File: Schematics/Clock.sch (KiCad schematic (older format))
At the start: 27 parts, among them SW1 SW_Push, U66 LM555, U67 74LS393, U68 74LS04, U69 74LS393, U70 74LS151, U71 74LS393, U72 74LS393, U73 74LS393, U74 74LS393

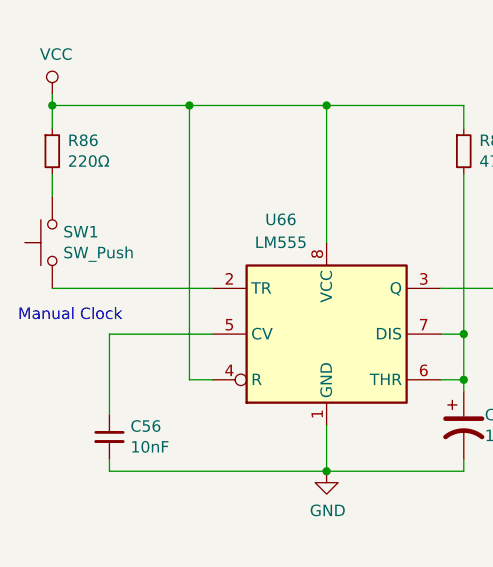
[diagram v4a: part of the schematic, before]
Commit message: Assign a bunch of part footprints.
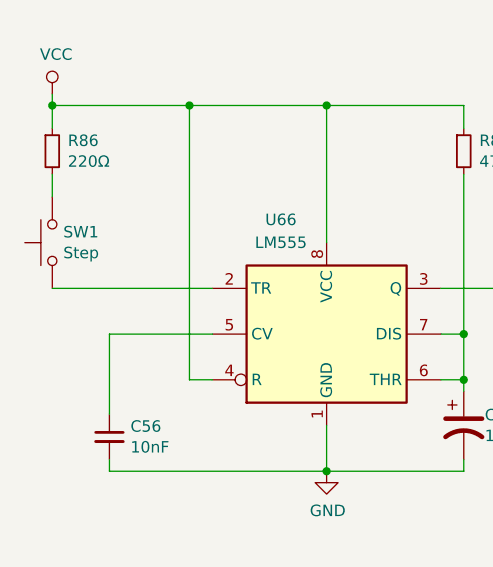
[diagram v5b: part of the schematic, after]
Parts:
- D72: footprint (none) -> LED_THT:LED_D5.0mm
- R86, R87, R88: footprint (none) -> Resistor_THT:R_Axial_DIN0207_L6.3mm_D2.5mm_P7.62mm_Horizontal
- SW1: value SW_Push -> Step; footprint (none) -> Button_Switch_THT:SW_PUSH_6mm_H5mm
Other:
- note removed: "Manual Clock"
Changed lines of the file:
@@
 F 0 "R88" H 5118 6046 50  0000 L CNN
 F 1 "220Ω" H 5118 5955 50  0000 L CNN
-F 2 "" V 5090 5990 50  0001 C CNN
+F 2 "Resistor_THT:R_Axial_DIN0207_L6.3mm_D2.5mm_P7.62mm_Horizontal" V 5090 5990 50  0001 C CNN
 F 3 "~" H 5050 6000 50  0001 C CNN
 	1    5050 6000
@@
 F 0 "D72" V 5089 5433 50  0000 R CNN
 F 1 "LED" V 4998 5433 50  0000 R CNN
-F 2 "" H 5050 5550 50  0001 C CNN
+F 2 "LED_THT:LED_D5.0mm" H 5050 5550 50  0001 C CNN
 F 3 "~" H 5050 5550 50  0001 C CNN
 	1    5050 5550
@@
 F 0 "R87" H 2668 3396 50  0000 L CNN
 F 1 "47kΩ" H 2668 3305 50  0000 L CNN
-F 2 "" H 2600 3350 50  0001 C CNN
+F 2 "Resistor_THT:R_Axial_DIN0207_L6.3mm_D2.5mm_P7.62mm_Horizontal" H 2600 3350 50  0001 C CNN
 F 3 "~" H 2600 3350 50  0001 C CNN
 	1    2600 3350
@@
 F 0 "R86" H 868 3396 50  0000 L CNN
 F 1 "220Ω" H 868 3305 50  0000 L CNN
-F 2 "" H 800 3350 50  0001 C CNN
+F 2 "Resistor_THT:R_Axial_DIN0207_L6.3mm_D2.5mm_P7.62mm_Horizontal" H 800 3350 50  0001 C CNN
 F 3 "~" H 800 3350 50  0001 C CNN
 	1    800  3350
@@
 P 800 3750
 F 0 "SW1" V 846 3702 50  0000 R CNN
-F 1 "SW_Push" V 755 3702 50  0000 R CNN
-F 2 "" H 800 3950 50  0001 C CNN
+F 1 "Step" V 755 3702 50  0000 R CNN
+F 2 "Button_Switch_THT:SW_PUSH_6mm_H5mm" H 800 3950 50  0001 C CNN
 F 3 "~" H 800 3950 50  0001 C CNN
 	1    800  3750
 	0    -1   -1   0
 $EndComp
-Text Notes 650  4100 0    50   ~ 0
-Manual Clock
 Wire Wire Line
 	3650 5200 3150 5200

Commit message: Assign a bunch more footprints. All are assigned now.
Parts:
- U66: footprint (none) -> Package_DIP:DIP-8_W7.62mm
- U67, U68, U69, U71, U72, U73, U74: footprint (none) -> Package_DIP:DIP-14_W7.62mm
- U70: footprint (none) -> Package_DIP:DIP-16_W7.62mm
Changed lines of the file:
@@
 F 0 "U67" H 2550 1917 50  0000 C CNN
 F 1 "74LS393" H 2550 1826 50  0000 C CNN
-F 2 "" H 2550 1550 50  0001 C CNN
+F 2 "Package_DIP:DIP-14_W7.62mm" H 2550 1550 50  0001 C CNN
 F 3 "74xx\\74LS393.pdf" H 2550 1550 50  0001 C CNN
 	1    2550 1550
@@
 F 0 "U71" H 5300 1917 50  0000 C CNN
 F 1 "74LS393" H 5300 1826 50  0000 C CNN
-F 2 "" H 5300 1550 50  0001 C CNN
+F 2 "Package_DIP:DIP-14_W7.62mm" H 5300 1550 50  0001 C CNN
 F 3 "74xx\\74LS393.pdf" H 5300 1550 50  0001 C CNN
 	1    5300 1550
@@
 F 0 "U72" H 6600 1917 50  0000 C CNN
 F 1 "74LS393" H 6600 1826 50  0000 C CNN
-F 2 "" H 6600 1550 50  0001 C CNN
+F 2 "Package_DIP:DIP-14_W7.62mm" H 6600 1550 50  0001 C CNN
 F 3 "74xx\\74LS393.pdf" H 6600 1550 50  0001 C CNN
 	1    6600 1550
@@
 F 0 "U73" H 7950 1917 50  0000 C CNN
 F 1 "74LS393" H 7950 1826 50  0000 C CNN
-F 2 "" H 7950 1550 50  0001 C CNN
+F 2 "Package_DIP:DIP-14_W7.62mm" H 7950 1550 50  0001 C CNN
 F 3 "74xx\\74LS393.pdf" H 7950 1550 50  0001 C CNN
 	1    7950 1550
@@
 F 0 "U74" H 9350 1917 50  0000 C CNN
 F 1 "74LS393" H 9350 1826 50  0000 C CNN
-F 2 "" H 9350 1550 50  0001 C CNN
+F 2 "Package_DIP:DIP-14_W7.62mm" H 9350 1550 50  0001 C CNN
 F 3 "74xx\\74LS393.pdf" H 9350 1550 50  0001 C CNN
 	1    9350 1550
@@
 F 0 "U69" H 3900 1917 50  0000 C CNN
 F 1 "74LS393" H 3900 1826 50  0000 C CNN
-F 2 "" H 3900 1550 50  0001 C CNN
+F 2 "Package_DIP:DIP-14_W7.62mm" H 3900 1550 50  0001 C CNN
 F 3 "74xx\\74LS393.pdf" H 3900 1550 50  0001 C CNN
 	1    3900 1550
@@
 F 0 "U70" H 3900 6400 50  0000 C CNN
 F 1 "74LS151" H 3900 6300 50  0000 C CNN
-F 2 "" H 4150 5500 50  0001 C CNN
+F 2 "Package_DIP:DIP-16_W7.62mm" H 4150 5500 50  0001 C CNN
 F 3 "http://www.ti.com/lit/gpn/sn74LS151" H 4150 5500 50  0001 C CNN
 	1    4150 5500
@@
 F 0 "U68" H 2800 6767 50  0000 C CNN
 F 1 "74LS04" H 2800 6676 50  0000 C CNN
-F 2 "" H 2800 6450 50  0001 C CNN
+F 2 "Package_DIP:DIP-14_W7.62mm" H 2800 6450 50  0001 C CNN
 F 3 "http://www.ti.com/lit/gpn/sn74LS04" H 2800 6450 50  0001 C CNN
 	1    2800 6450
@@
 F 0 "U66" H 1800 4650 50  0000 C CNN
 F 1 "LM555" H 1800 4550 50  0000 C CNN
-F 2 "" H 2000 4150 50  0001 C CNN
+F 2 "Package_DIP:DIP-8_W7.62mm" H 2000 4150 50  0001 C CNN
 F 3 "http://www.ti.com/lit/ds/symlink/lm555.pdf" H 2000 4150 50  0001 C CNN
 	1    2000 4150

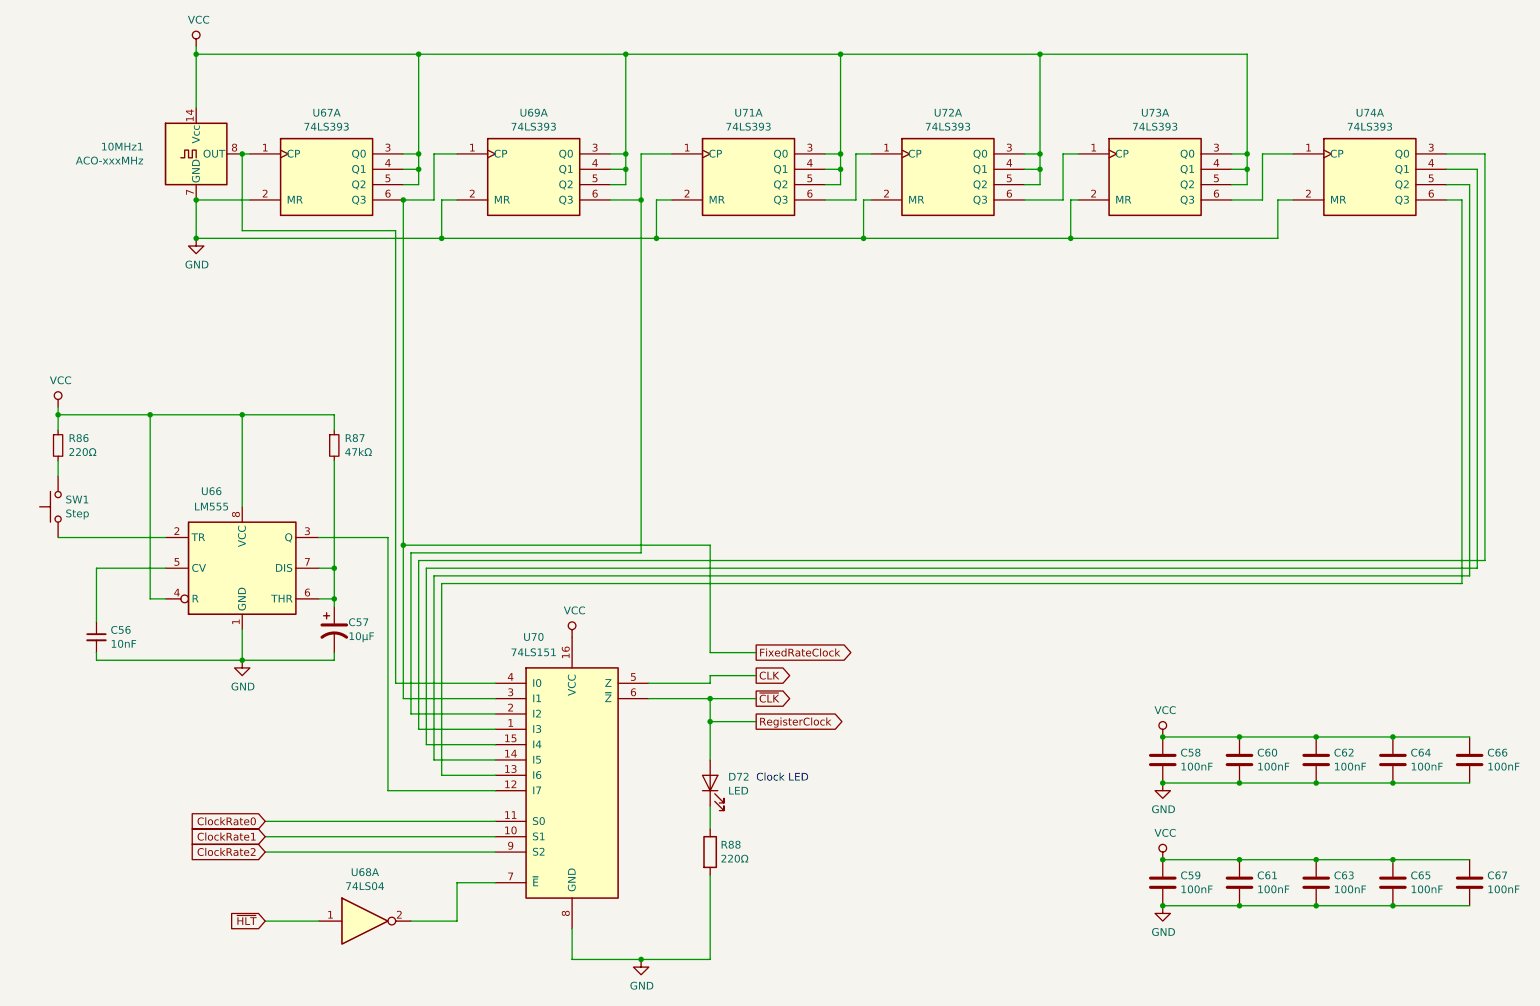
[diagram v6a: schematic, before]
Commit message: Add unused IC units to Output Display to ensure no ICs are shared with other modules.
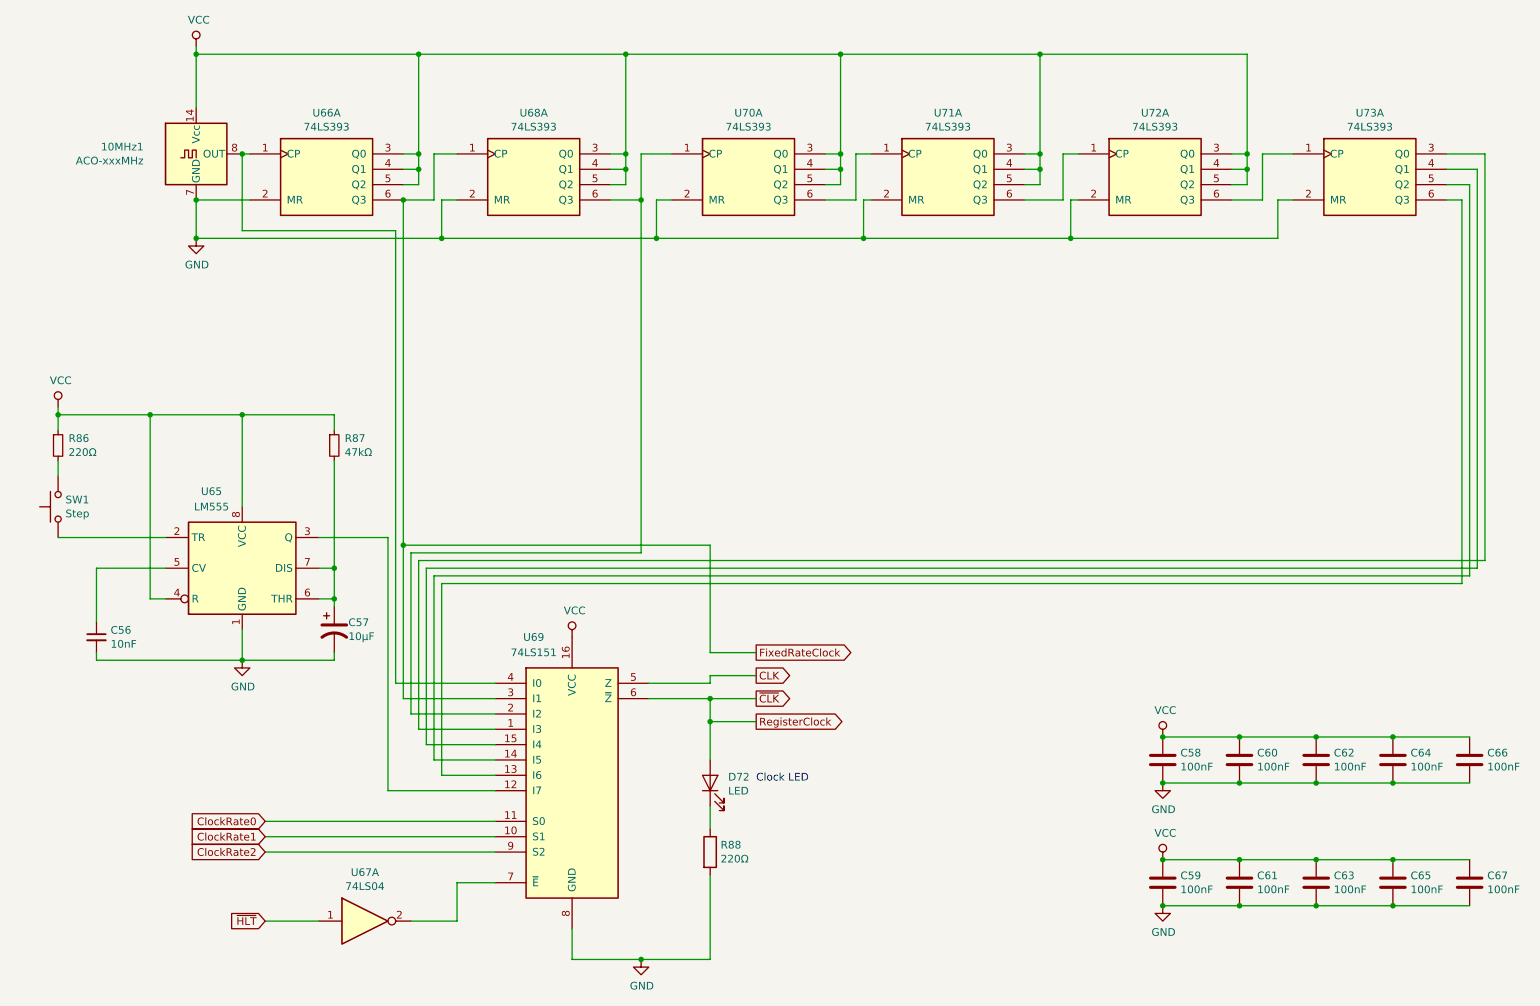
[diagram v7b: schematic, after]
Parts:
- renumbered U66 to U65, U67 to U66, U68 to U67, U69 to U68, U70 to U69, U71 to U70, U72 to U71, U73 to U72, U74 to U73
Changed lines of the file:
@@
 $EndComp
 $Comp
-L 74xx:74LS393 U67
+L 74xx:74LS393 U66
 U 1 1 5D3898BC
 P 2550 1550
-F 0 "U67" H 2550 1917 50  0000 C CNN
+F 0 "U66" H 2550 1917 50  0000 C CNN
 F 1 "74LS393" H 2550 1826 50  0000 C CNN
 F 2 "Package_DIP:DIP-14_W7.62mm" H 2550 1550 50  0001 C CNN
@@
 $EndComp
 $Comp
-L 74xx:74LS393 U71
+L 74xx:74LS393 U70
 U 1 1 5D38C231
 P 5300 1550
-F 0 "U71" H 5300 1917 50  0000 C CNN
+F 0 "U70" H 5300 1917 50  0000 C CNN
 F 1 "74LS393" H 5300 1826 50  0000 C CNN
 F 2 "Package_DIP:DIP-14_W7.62mm" H 5300 1550 50  0001 C CNN
@@
 $EndComp
 $Comp
-L 74xx:74LS393 U72
+L 74xx:74LS393 U71
 U 1 1 5D38D960
 P 6600 1550
-F 0 "U72" H 6600 1917 50  0000 C CNN
+F 0 "U71" H 6600 1917 50  0000 C CNN
 F 1 "74LS393" H 6600 1826 50  0000 C CNN
 F 2 "Package_DIP:DIP-14_W7.62mm" H 6600 1550 50  0001 C CNN
@@
 $EndComp
 $Comp
-L 74xx:74LS393 U73
+L 74xx:74LS393 U72
 U 1 1 5D38E544
 P 7950 1550
-F 0 "U73" H 7950 1917 50  0000 C CNN
+F 0 "U72" H 7950 1917 50  0000 C CNN
 F 1 "74LS393" H 7950 1826 50  0000 C CNN
 F 2 "Package_DIP:DIP-14_W7.62mm" H 7950 1550 50  0001 C CNN
@@
 	7350 1450 7450 1450
 $Comp
-L 74xx:74LS393 U74
+L 74xx:74LS393 U73
 U 1 1 5D3C15D2
 P 9350 1550
-F 0 "U74" H 9350 1917 50  0000 C CNN
+F 0 "U73" H 9350 1917 50  0000 C CNN
 F 1 "74LS393" H 9350 1826 50  0000 C CNN
 F 2 "Package_DIP:DIP-14_W7.62mm" H 9350 1550 50  0001 C CNN
@@
 Connection ~ 7200 800
 $Comp
-L 74xx:74LS393 U69
+L 74xx:74LS393 U68
 U 1 1 5D38B39F
 P 3900 1550
-F 0 "U69" H 3900 1917 50  0000 C CNN
+F 0 "U68" H 3900 1917 50  0000 C CNN
 F 1 "74LS393" H 3900 1826 50  0000 C CNN
 F 2 "Package_DIP:DIP-14_W7.62mm" H 3900 1550 50  0001 C CNN
@@
 	1700 1750 2050 1750
 $Comp
-L 74xx:74LS151 U70
+L 74xx:74LS151 U69
 U 1 1 5D3FEA17
 P 4150 5500
-F 0 "U70" H 3900 6400 50  0000 C CNN
+F 0 "U69" H 3900 6400 50  0000 C CNN
 F 1 "74LS151" H 3900 6300 50  0000 C CNN
 F 2 "Package_DIP:DIP-16_W7.62mm" H 4150 5500 50  0001 C CNN
@@
 	5050 4850 5350 4850
 $Comp
-L power:VCC #PWR0249
+L power:VCC #PWR0153
 U 1 1 5D90C7E6
 P 4150 4600
-F 0 "#PWR0249" H 4150 4450 50  0001 C CNN
+F 0 "#PWR0153" H 4150 4450 50  0001 C CNN
 F 1 "VCC" H 4167 4773 50  0000 C CNN
 F 2 "" H 4150 4600 50  0001 C CNN
@@
 $EndComp
 $Comp
-L power:GND #PWR0250
+L power:GND #PWR0152
 U 1 1 5D919C2F
 P 2000 4750
-F 0 "#PWR0250" H 2000 4500 50  0001 C CNN
+F 0 "#PWR0152" H 2000 4500 50  0001 C CNN
 F 1 "GND" H 2005 4577 50  0000 C CNN
 F 2 "" H 2000 4750 50  0001 C CNN
@@
 $EndComp
 $Comp
-L power:GND #PWR0251
+L power:GND #PWR0154
 U 1 1 5D91A0CA
 P 4600 6700
-F 0 "#PWR0251" H 4600 6450 50  0001 C CNN
+F 0 "#PWR0154" H 4600 6450 50  0001 C CNN
 F 1 "GND" H 4605 6527 50  0000 C CNN
 F 2 "" H 4600 6700 50  0001 C CNN
@@
 $EndComp
 $Comp
-L power:GND #PWR0252
+L power:GND #PWR0156
 U 1 1 5D936CDD
 P 8000 5550
-F 0 "#PWR0252" H 8000 5300 50  0001 C CNN
+F 0 "#PWR0156" H 8000 5300 50  0001 C CNN
 F 1 "GND" H 8005 5377 50  0000 C CNN
 F 2 "" H 8000 5550 50  0001 C CNN
@@
 $EndComp
 $Comp
-L power:VCC #PWR0253
+L power:VCC #PWR0155
 U 1 1 5D937A39
 P 8000 5250
-F 0 "#PWR0253" H 8000 5100 50  0001 C CNN
+F 0 "#PWR0155" H 8000 5100 50  0001 C CNN
 F 1 "VCC" H 8017 5423 50  0000 C CNN
 F 2 "" H 8000 5250 50  0001 C CNN
@@
 $EndComp
 $Comp
-L power:GND #PWR0254
+L power:GND #PWR0158
 U 1 1 5D9721F9
 P 8000 6350
-F 0 "#PWR0254" H 8000 6100 50  0001 C CNN
+F 0 "#PWR0158" H 8000 6100 50  0001 C CNN
 F 1 "GND" H 8005 6177 50  0000 C CNN
 F 2 "" H 8000 6350 50  0001 C CNN
@@
 $EndComp
 $Comp
-L power:VCC #PWR0255
+L power:VCC #PWR0157
 U 1 1 5D9721FF
 P 8000 6050
-F 0 "#PWR0255" H 8000 5900 50  0001 C CNN
+F 0 "#PWR0157" H 8000 5900 50  0001 C CNN
 F 1 "VCC" H 8017 6223 50  0000 C CNN
 F 2 "" H 8000 6050 50  0001 C CNN
@@
 	3300 1750 3300 2000
 $Comp
-L power:GND #PWR0256
+L power:GND #PWR0151
 U 1 1 5D888695
 P 1700 2000
-F 0 "#PWR0256" H 1700 1750 50  0001 C CNN
+F 0 "#PWR0151" H 1700 1750 50  0001 C CNN
 F 1 "GND" H 1705 1827 50  0000 C CNN
 F 2 "" H 1700 2000 50  0001 C CNN
@@
 	1700 2000 3300 2000
 $Comp
-L power:VCC #PWR0257
+L power:VCC #PWR0150
 U 1 1 5D3986DC
 P 1700 750
-F 0 "#PWR0257" H 1700 600 50  0001 C CNN
+F 0 "#PWR0150" H 1700 600 50  0001 C CNN
 F 1 "VCC" H 1717 923 50  0000 C CNN
 F 2 "" H 1700 750 50  0001 C CNN
@@
 	1700 750  1700 800
 $Comp
-L power:VCC #PWR0258
+L power:VCC #PWR0149
 U 1 1 5D8FB444
 P 800 3100
-F 0 "#PWR0258" H 800 2950 50  0001 C CNN
+F 0 "#PWR0149" H 800 2950 50  0001 C CNN
 F 1 "VCC" H 817 3273 50  0000 C CNN
 F 2 "" H 800 3100 50  0001 C CNN
@@
 	3100 6450 3400 6450
 $Comp
-L 74xx:74LS04 U68
+L 74xx:74LS04 U67
 U 1 1 5D7C9FC5
 P 2800 6450
-F 0 "U68" H 2800 6767 50  0000 C CNN
+F 0 "U67" H 2800 6767 50  0000 C CNN
 F 1 "74LS04" H 2800 6676 50  0000 C CNN
 F 2 "Package_DIP:DIP-14_W7.62mm" H 2800 6450 50  0001 C CNN
@@
 	4600 6700 5050 6700
 $Comp
-L Timer:LM555 U66
+L Timer:LM555 U65
 U 1 1 5D38F3A1
 P 2000 4150
-F 0 "U66" H 1800 4650 50  0000 C CNN
+F 0 "U65" H 1800 4650 50  0000 C CNN
 F 1 "LM555" H 1800 4550 50  0000 C CNN
 F 2 "Package_DIP:DIP-8_W7.62mm" H 2000 4150 50  0001 C CNN

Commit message: Add unused IC units to Data RAM to ensure no ICs are shared with other modules.
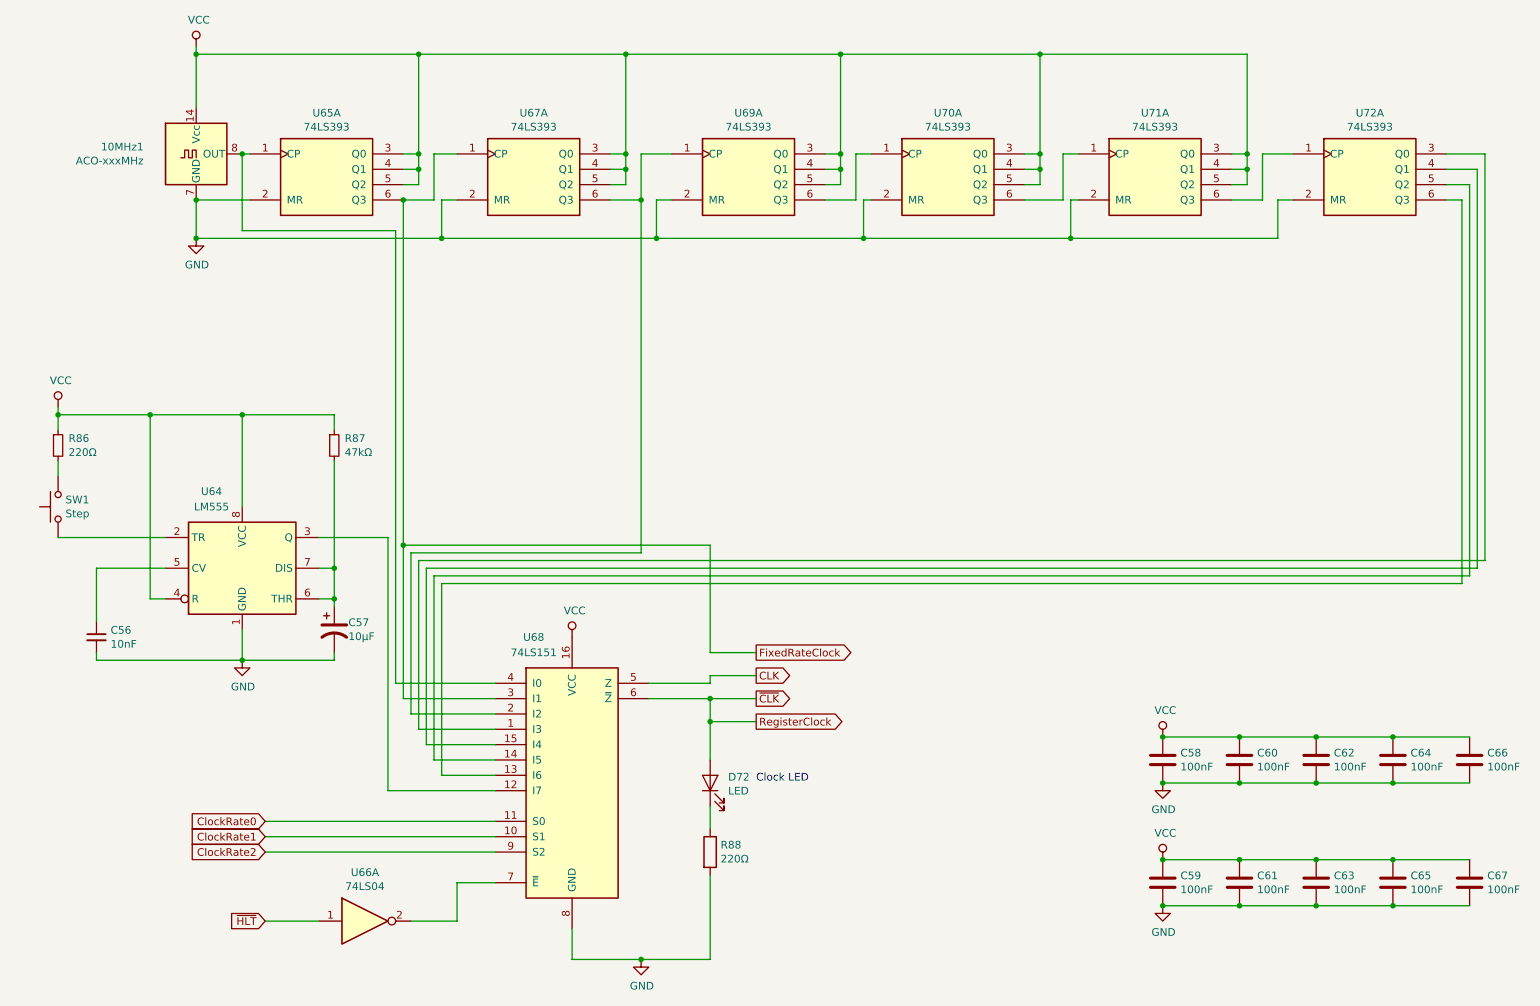
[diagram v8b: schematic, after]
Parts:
- renumbered U65 to U64, U66 to U65, U67 to U66, U68 to U67, U69 to U68, U70 to U69, U71 to U70, U72 to U71, U73 to U72
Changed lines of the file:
@@
 $EndComp
 $Comp
-L 74xx:74LS393 U66
+L 74xx:74LS393 U65
 U 1 1 5D3898BC
 P 2550 1550
-F 0 "U66" H 2550 1917 50  0000 C CNN
+F 0 "U65" H 2550 1917 50  0000 C CNN
 F 1 "74LS393" H 2550 1826 50  0000 C CNN
 F 2 "Package_DIP:DIP-14_W7.62mm" H 2550 1550 50  0001 C CNN
@@
 $EndComp
 $Comp
-L 74xx:74LS393 U70
+L 74xx:74LS393 U69
 U 1 1 5D38C231
 P 5300 1550
-F 0 "U70" H 5300 1917 50  0000 C CNN
+F 0 "U69" H 5300 1917 50  0000 C CNN
 F 1 "74LS393" H 5300 1826 50  0000 C CNN
 F 2 "Package_DIP:DIP-14_W7.62mm" H 5300 1550 50  0001 C CNN
@@
 $EndComp
 $Comp
-L 74xx:74LS393 U71
+L 74xx:74LS393 U70
 U 1 1 5D38D960
 P 6600 1550
-F 0 "U71" H 6600 1917 50  0000 C CNN
+F 0 "U70" H 6600 1917 50  0000 C CNN
 F 1 "74LS393" H 6600 1826 50  0000 C CNN
 F 2 "Package_DIP:DIP-14_W7.62mm" H 6600 1550 50  0001 C CNN
@@
 $EndComp
 $Comp
-L 74xx:74LS393 U72
+L 74xx:74LS393 U71
 U 1 1 5D38E544
 P 7950 1550
-F 0 "U72" H 7950 1917 50  0000 C CNN
+F 0 "U71" H 7950 1917 50  0000 C CNN
 F 1 "74LS393" H 7950 1826 50  0000 C CNN
 F 2 "Package_DIP:DIP-14_W7.62mm" H 7950 1550 50  0001 C CNN
@@
 	7350 1450 7450 1450
 $Comp
-L 74xx:74LS393 U73
+L 74xx:74LS393 U72
 U 1 1 5D3C15D2
 P 9350 1550
-F 0 "U73" H 9350 1917 50  0000 C CNN
+F 0 "U72" H 9350 1917 50  0000 C CNN
 F 1 "74LS393" H 9350 1826 50  0000 C CNN
 F 2 "Package_DIP:DIP-14_W7.62mm" H 9350 1550 50  0001 C CNN
@@
 Connection ~ 7200 800
 $Comp
-L 74xx:74LS393 U68
+L 74xx:74LS393 U67
 U 1 1 5D38B39F
 P 3900 1550
-F 0 "U68" H 3900 1917 50  0000 C CNN
+F 0 "U67" H 3900 1917 50  0000 C CNN
 F 1 "74LS393" H 3900 1826 50  0000 C CNN
 F 2 "Package_DIP:DIP-14_W7.62mm" H 3900 1550 50  0001 C CNN
@@
 	1700 1750 2050 1750
 $Comp
-L 74xx:74LS151 U69
+L 74xx:74LS151 U68
 U 1 1 5D3FEA17
 P 4150 5500
-F 0 "U69" H 3900 6400 50  0000 C CNN
+F 0 "U68" H 3900 6400 50  0000 C CNN
 F 1 "74LS151" H 3900 6300 50  0000 C CNN
 F 2 "Package_DIP:DIP-16_W7.62mm" H 4150 5500 50  0001 C CNN
@@
 	3100 6450 3400 6450
 $Comp
-L 74xx:74LS04 U67
+L 74xx:74LS04 U66
 U 1 1 5D7C9FC5
 P 2800 6450
-F 0 "U67" H 2800 6767 50  0000 C CNN
+F 0 "U66" H 2800 6767 50  0000 C CNN
 F 1 "74LS04" H 2800 6676 50  0000 C CNN
 F 2 "Package_DIP:DIP-14_W7.62mm" H 2800 6450 50  0001 C CNN
@@
 	4600 6700 5050 6700
 $Comp
-L Timer:LM555 U65
+L Timer:LM555 U64
 U 1 1 5D38F3A1
 P 2000 4150
-F 0 "U65" H 1800 4650 50  0000 C CNN
+F 0 "U64" H 1800 4650 50  0000 C CNN
 F 1 "LM555" H 1800 4550 50  0000 C CNN
 F 2 "Package_DIP:DIP-8_W7.62mm" H 2000 4150 50  0001 C CNN
